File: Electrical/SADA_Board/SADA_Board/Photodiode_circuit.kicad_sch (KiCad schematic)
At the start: 34 parts

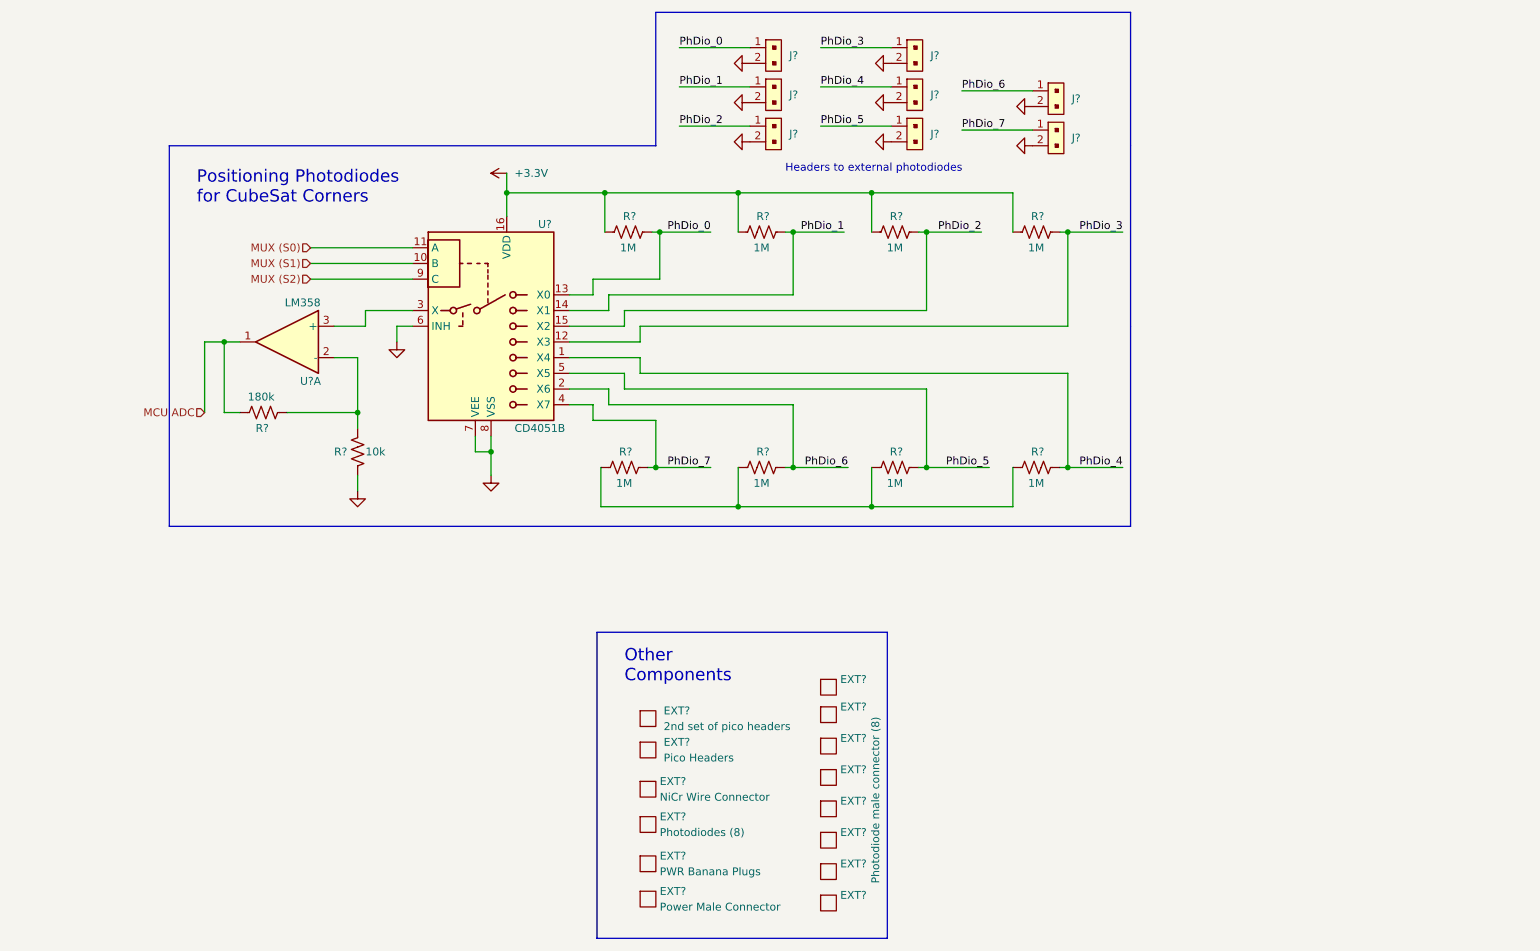
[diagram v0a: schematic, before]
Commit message: Partial implementation of stepper motor Step up
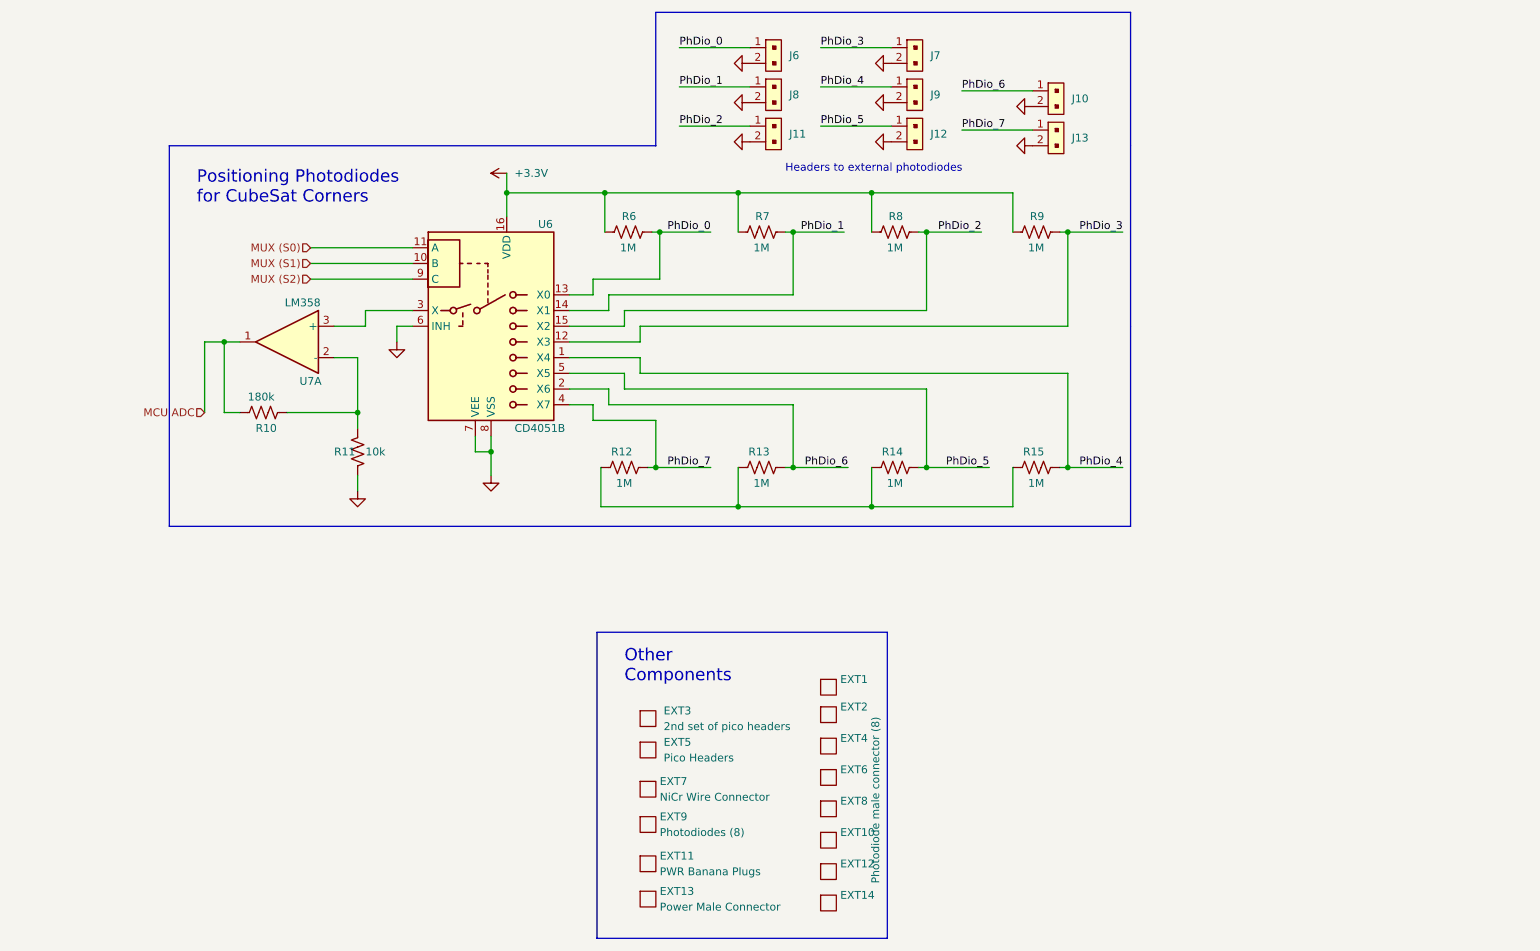
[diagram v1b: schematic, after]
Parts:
- gave numbers to parts that had none: 34

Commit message: Connectors, Oscillator
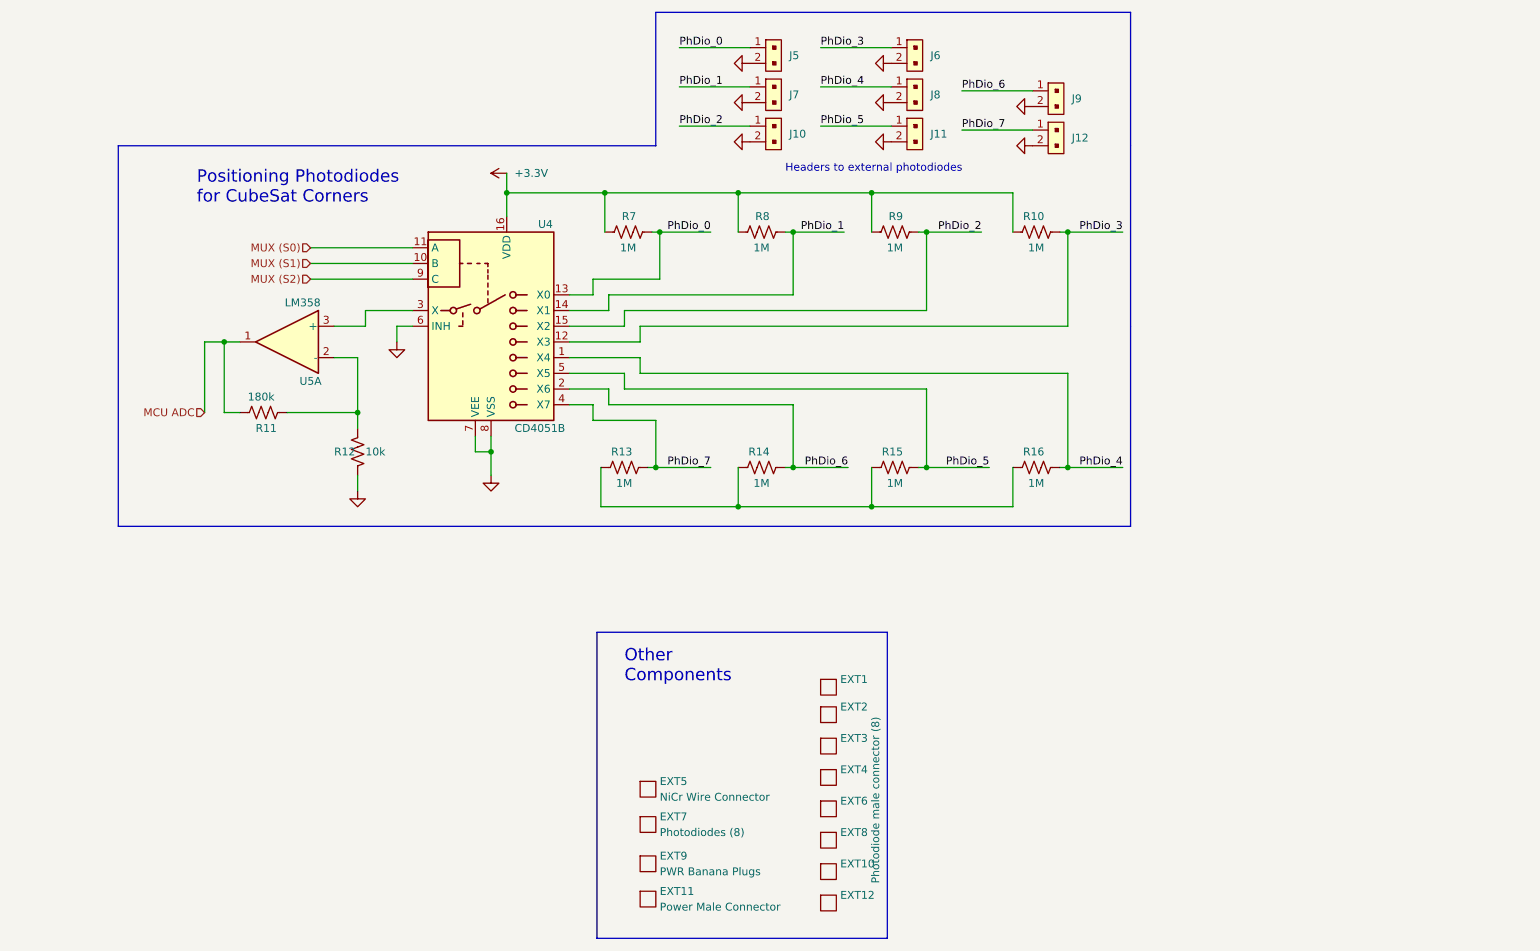
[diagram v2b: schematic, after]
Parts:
- removed EXT3: 2nd set of pico headers, 0_custom:EXT_no_footprint, symbol 0_custom:{lt}name{gt}
- removed EXT5: Pico Headers, 0_custom:EXT_no_footprint, symbol 0_custom:{lt}name{gt}
- U5: renamed from U7; MPN LM358MX -> LM358MX/NOPB
- renumbered EXT12 to EXT10, EXT13 to EXT11, EXT14 to EXT12, EXT4 to EXT3, EXT6 to EXT4, EXT7 to EXT5, EXT8 to EXT6, EXT9 to EXT7, EXT10 to EXT8, EXT11 to EXT9, J11 to J10, J12 to J11, J13 to J12, J6 to J5, J7 to J6, J8 to J7, J9 to J8, J10 to J9, R9 to R10, R10 to R11, R11 to R12, R12 to R13, R13 to R14, R14 to R15, R15 to R16, R6 to R7, R7 to R8, R8 to R9, U6 to U4

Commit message: Pre-Design Review II
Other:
- moved on the sheet: EXT1, EXT10, EXT11, EXT12, EXT2, EXT3, EXT4, EXT5, EXT6, EXT7, EXT8, EXT9

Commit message: Pre-passive retainment change
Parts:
- removed EXT10, EXT12, EXT2, EXT3, EXT4, EXT6, EXT8: Photodiode male connector (8), 0_custom:EXT_no_footprint, symbol 0_custom:{lt}name{gt}
- removed EXT11: Power Male Connector, 0_custom:EXT_no_footprint, symbol 0_custom:{lt}name{gt}
- removed EXT5: NiCr Wire Connector, 0_custom:EXT_no_footprint, symbol 0_custom:{lt}name{gt}
- removed EXT9: PWR Banana Plugs, 0_custom:EXT_no_footprint, symbol 0_custom:{lt}name{gt}
- removed R10, R13, R14, R15, R16, R7, R8, R9: 1M, Resistor_SMD:R_0805_2012Metric_Pad1.20x1.40mm_HandSolder, symbol Device:R_US
- removed R12: 10k, Resistor_SMD:R_0805_2012Metric_Pad1.20x1.40mm_HandSolder, symbol Device:R_US
- removed U5: LM358, Miles Added:M08A-L, symbol Amplifier_Operational:LM358
- added C?: 10 nF, Capacitor_SMD:C_0402_1005Metric, symbol Device:C
- added C?: 1nF, Resistor_SMD:R_0402_1005Metric, symbol Device:C
- added U?: LM321, Package_TO_SOT_SMD:SOT-23-5, symbol Amplifier_Operational:LMV321
- EXT7: MPN (none) -> SFH 203 P
- R11: value 180k -> 200k; footprint Resistor_SMD:R_0805_2012Metric_Pad1.20x1.40mm_HandSolder -> Resistor_SMD:R_0603_1608Metric_Pad0.98x0.95mm_HandSolder; MPN RC0805FR-07182KL -> AC0603FR-07200KL; Name (none) -> Rf
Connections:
- net GND: now also C?.2, U?.1 (+), U?.2 (V-)
- net MCU ADC: now also U?.4; no longer R11.2
- net at R11.1: now also U4.3 (X), C?.1, C?.2, U?.3 (-)
- net +3.3V renamed +3V3
- net +3V3: now also U?.5 (V+)
- new net: C?.1, R11.2
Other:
- note added: "Image reflects a negative V_out, though in circuit photodiode polarity should be reversed"
- note added: "Schematic Notes - DNS = Do Not Solder. These photodiodes are not implemented at this time, though functionality is implemented to the board for future uses - Example attitude determination photodiodes are SFH 203 P, and supporting circuitry designed around those. Please adjust R_F and buffer capacitor accordingly"
- note removed: "Other Components"
- note removed: "Positioning Photodiodes for CubeSat Corners"
- moved on the sheet: EXT1, EXT7, J10, J11, J12, J5, J6, J7, J8, J9, R11, U4

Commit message: pre-gio review
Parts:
- removed EXT1: Photodiode male connector (8), 0_custom:EXT_no_footprint, symbol 0_custom:{lt}name{gt}
- removed J10, J11, J12, J5, J6, J7, J8, J9: B2B-PH-K-S_LF__SN_, digikey-footprints:PinHeader_1x2_P2mm_Drill1mm, symbol dk_Rectangular-Connectors-Headers-Male-Pins:B2B-PH-K-S_LF__SN_
- added D8: TVS, symbol Diode:ESD5Zxx
- added EXT4: Male Connector, 0_custom:EXT_no_footprint, symbol 0_custom:{lt}name{gt}
- added J6: Conn_01x16, Miles Added:CON16_1X16_DUH_HPI125_TYC, symbol Connector_Generic:Conn_01x16
- added TP5, TP6: TestPoint, TestPoint:TestPoint_Pad_D1.5mm, symbol Connector:TestPoint
- gave numbers to parts that had none: 3
- renumbered EXT7 to EXT5, R11 to R3, U4 to U2
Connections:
- net GND: now also D8.2 (A), J6.10 (Pin_10), J6.12 (Pin_12), J6.14 (Pin_14), J6.16 (Pin_16), J6.2 (Pin_2), J6.4 (Pin_4), J6.6 (Pin_6), J6.8 (Pin_8)
- net PhDio_0: now also J6.1 (Pin_1)
- net PhDio_1: now also J6.3 (Pin_3)
- net PhDio_2: now also J6.5 (Pin_5)
- net PhDio_3: now also J6.7 (Pin_7)
- net PhDio_4: now also J6.9 (Pin_9)
- net PhDio_5: now also J6.11 (Pin_11)
- net PhDio_6: now also J6.13 (Pin_13)
- net PhDio_7: now also J6.15 (Pin_15)
- net at C10.2, C11.1, R3.1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: now also D8.1 (K), TP6.1
- net at C10.1, R3.2: now also TP5.1
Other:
- moved on the sheet: C10, C11, EXT5, R3, U2, U3

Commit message: ESD changes
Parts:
- D8: footprint (none) -> Diode_SMD:D_0402_1005Metric
- TP5, TP6: footprint TestPoint:TestPoint_Pad_D1.5mm -> TestPoint:TestPoint_Pad_D1.0mm
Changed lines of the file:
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@@
       (effects (font (size 1.27 1.27)) (justify right) hide)
     )
-    (property "Footprint" "TestPoint:TestPoint_Pad_D1.5mm" (id 2) (at 71.755 69.6775 0)
+    (property "Footprint" "TestPoint:TestPoint_Pad_D1.0mm" (id 2) (at 71.755 69.6775 0)
       (effects (font (size 1.27 1.27)) hide)
     )
@@
       (effects (font (size 1.27 1.27)) (justify right) hide)
     )
-    (property "Footprint" "TestPoint:TestPoint_Pad_D1.5mm" (id 2) (at 106.934 82.296 0)
+    (property "Footprint" "TestPoint:TestPoint_Pad_D1.0mm" (id 2) (at 106.934 82.296 0)
       (effects (font (size 1.27 1.27)) hide)
     )
@@
       (effects (font (size 1.27 1.27)) hide)
     )
-    (property "Footprint" "" (id 2) (at 103.251 89.408 0)
+    (property "Footprint" "Diode_SMD:D_0402_1005Metric" (id 2) (at 103.251 89.408 0)
       (effects (font (size 1.27 1.27)) hide)
     )

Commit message: V1.0 Finished
Submitted to manufacturing.
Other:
- note added: "Cathodes"
- note added: "Ground Anodes"
- note added: "Schematic Notes - DNS = Do Not Solder. These photodiodes are not implemented at this time, though functionality is implemented to the board for future uses - Example attitude determination photodiodes are SFH 203 P, and supporting circuitry designed around those. Please adjust R_F and buffer capacitor accordingly - Photodiodes work in photovoltaic mode: cathodes towards ADC, Anodes grounded"
- note removed: "Schematic Notes - DNS = Do Not Solder. These photodiodes are not implemented at this time, though functionality is implemented to the board for future uses - Example attitude determination photodiodes are SFH 203 P, and supporting circuitry designed around those. Please adjust R_F and buffer capacitor accordingly"
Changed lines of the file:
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@@
     (effects (font (size 1.27 1.27)) (justify left bottom))
   )
-  (text "Schematic Notes\n- DNS = Do Not Solder. These photodiodes are not implemented at this time, though\n	functionality is implemented to the board for future uses\n- Example attitude determination photodiodes are SFH 203 P, and supporting circuitry designed\n	around those. Please adjust R_F and buffer capacitor accordingly"
+  (text "Cathodes" (at 154.686 84.836 90)
+    (effects (font (size 1.27 1.27)) (justify left bottom))
+  )
+  (text "Ground Anodes" (at 191.516 87.884 90)
+    (effects (font (size 1.27 1.27)) (justify left bottom))
+  )
+  (text "Schematic Notes\n- DNS = Do Not Solder. These photodiodes are not implemented at this time, though\n	functionality is implemented to the board for future uses\n- Example attitude determination photodiodes are SFH 203 P, and supporting circuitry designed\n	around those. Please adjust R_F and buffer capacitor accordingly\n- Photodiodes work in photovoltaic mode: cathodes towards ADC, Anodes grounded"
     (at 16.51 171.323 0)
     (effects (font (size 1.27 1.27)) (justify left bottom))
@@
   )
   (symbol (lib_id "Connector_Generic:Conn_01x16") (at 187.198 74.676 0) (unit 1)
-    (in_bom yes) (on_board yes) (fields_autoplaced)
-    (property "Reference" "J6" (id 0) (at 189.992 74.6759 0)
+    (in_bom yes) (on_board yes)
+    (property "Reference" "J6" (id 0) (at 189.484 56.642 0)
       (effects (font (size 1.27 1.27)) (justify left))
     )

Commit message: Updated BOM
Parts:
- C11: value 10 nF -> 10nF
- D8: MPN (none) -> ESD321DPYR
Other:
- company: (none) -> Cal Poly, SLO
- title: (none) -> CubeSat SADA - Main
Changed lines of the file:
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@@
 (kicad_sch (version 20211123) (generator eeschema)
   (paper "A4")
+  (title_block
+    (title "CubeSat SADA - Main")
+    (date "2023-04-07")
+    (rev "V1.0")
+    (company "Cal Poly, SLO")
+  )
   (junction (at 107.696 82.296) (diameter 0) (color 0 0 0 0)
   )
@@
     (in_bom yes) (on_board yes)
     (property "Reference" "C11" (id 0) (at 100.203 85.725 0))
-    (property "Value" "10 nF" (id 1) (at 102.362 91.313 0))
+    (property "Value" "10nF" (id 1) (at 102.362 91.313 0))
     (property "Footprint" "Capacitor_SMD:C_0402_1005Metric" (id 2) (at 99.2632 92.71 0)
       (effects (font (size 1.27 1.27)) hide)
@@
       (effects (font (size 1.27 1.27)) hide)
     )
-    (property "MPN" "" (id 4) (at 107.696 89.408 0)
-      (effects (font (size 1.27 1.27)) hide)
-    )
+    (property "MPN" "ESD321DPYR" (id 4) (at 107.696 89.408 0)
+      (effects (font (size 1.27 1.27)) hide)
+    )
